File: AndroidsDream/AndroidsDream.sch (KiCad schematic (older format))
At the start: 9 parts, among them P1 LDR1, P2 LDR2, P3 LDR3, P4 Servo 1, P5 Servo 2, U1 ITSYBITSY

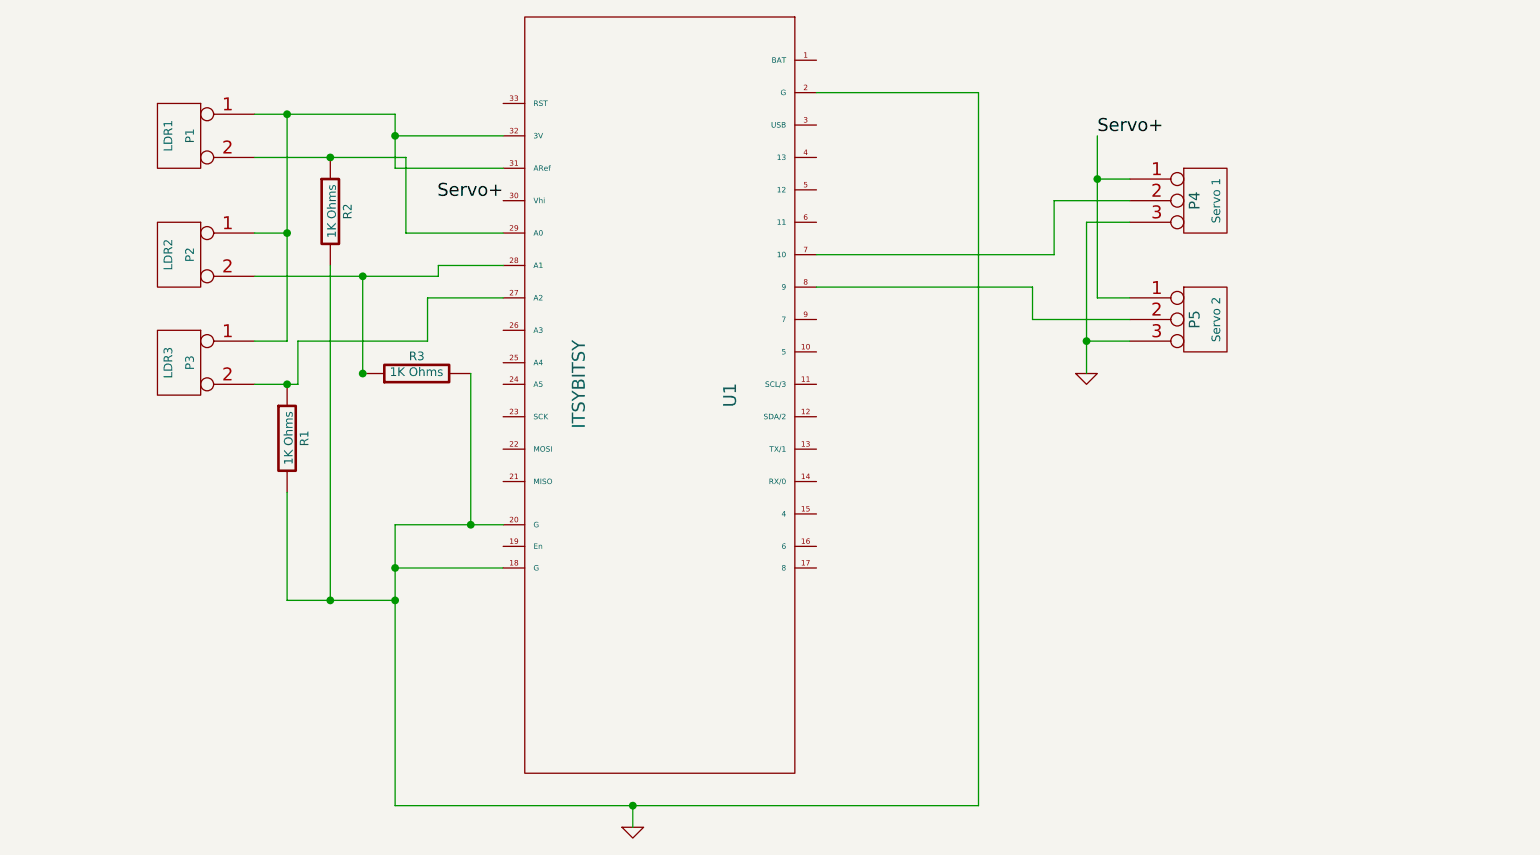
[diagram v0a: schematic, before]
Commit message: Add detailed comments to both the code and the schematics
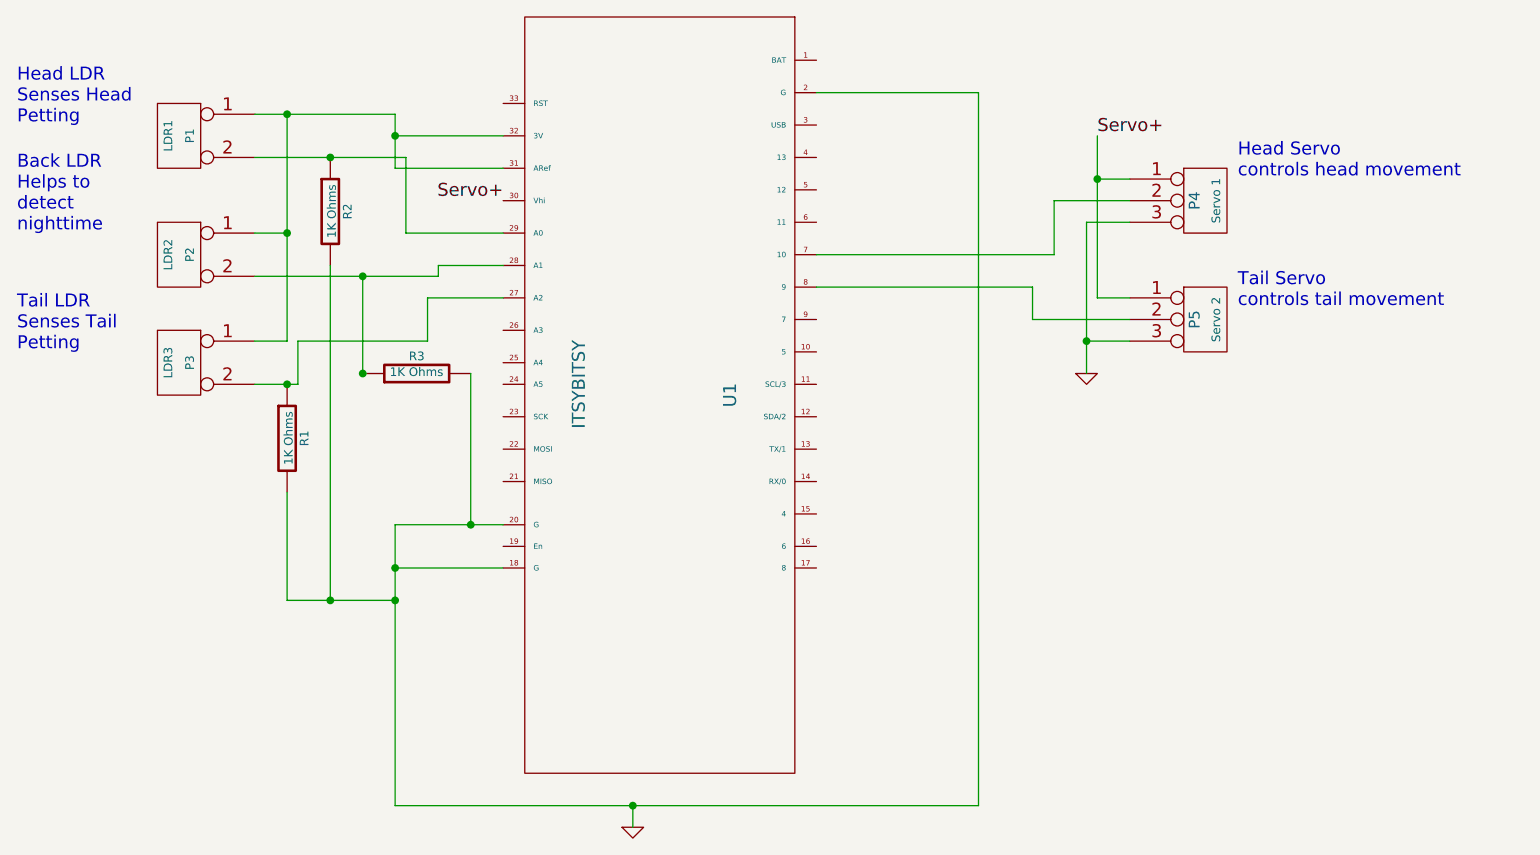
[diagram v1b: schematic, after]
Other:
- note added: "Back LDR\nHelps to \ndetect \nnighttime"
- note added: "Head LDR\nSenses Head \nPetting"
- note added: "Head Servo\ncontrols head movement"
- note added: "Tail LDR\nSenses Tail\nPetting"
- note added: "Tail Servo\ncontrols tail movement"
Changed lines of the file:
@@
 Sheet 1 1
 Title ""
-Date "4 nov 2018"
+Date "11 nov 2018"
 Rev ""
 Comp ""
@@
 	1850 3100 1850 3300
 Connection ~ 1800 3300
+Text Notes 6200 2350 0    60   ~ 0
+Head Servo\ncontrols head movement
+Text Notes 6200 2950 0    60   ~ 0
+Tail Servo\ncontrols tail movement
+Text Notes 550  2100 0    60   ~ 0
+Head LDR\nSenses Head \nPetting
+Text Notes 550  2600 0    60   ~ 0
+Back LDR\nHelps to \ndetect \nnighttime
+Text Notes 550  3150 0    60   ~ 0
+Tail LDR\nSenses Tail\nPetting
 $EndSCHEMATC
